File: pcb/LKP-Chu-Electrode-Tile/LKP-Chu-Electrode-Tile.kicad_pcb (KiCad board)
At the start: 2 copper layers, 19 parts, among them J1 Intercon, J10 Electrode 0, J11 Electrode 2, J12 Electrode 4, J13 Electrode 6, J14 Electrode 8, J15 Electrode 10, J16 Electrode 12, J17 Electrode 14, J2 Electrode 1, J3 Electrode 3, J4 Electrode 5, J5 Electrode 7, J6 Electrode 9, J7 Electrode 11, J8 Electrode 13, J9 Electrode 15

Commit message: Copper fills and fix solder mask on electrodes
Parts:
- J1: moved to B.Cu
- moved J1 201.1 mm to (240.6, 86.0)
- moved J6 144.1 mm to (217.2, 63.5)
- moved J8 133.4 mm to (113.2, 63.5)
- moved J5 117.4 mm to (243.2, 108.5)
- moved J10 106.7 mm to (61.2, 108.5)
- moved J16 98.3 mm to (139.2, 63.5)
- moved J4 93.5 mm to (191.2, 108.5)
- moved H1 89.2 mm to (33.5, 52.5)
- moved H2 89.2 mm to (20.6, 77.5)
- moved J9 87.0 mm to (61.2, 63.5)
- moved J11 83.4 mm to (113.2, 108.5)
- moved J14 75.3 mm to (243.2, 63.5)
- moved J7 75.3 mm to (165.2, 63.5)
- moved J3 71.2 mm to (139.2, 108.5)
- moved J12 62.2 mm to (165.2, 108.5)
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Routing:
- added copper zone on B.Cu, net (none)
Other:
- board outline added: 208.5 x 90 mm

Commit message: Place screw holes.
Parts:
- added H3: MountingHole, MountingHole:MountingHole_3.2mm_M3_ISO7380, F.Cu at (44.2, 86.0)
- moved H2 54.0 mm to (44.2, 126.0)
- moved H1 12.6 mm to (44.2, 46.0)
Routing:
- net Net-(J1-Pad10): track 0.00 -> 4.02 mm, vias 0 -> 1
- net Net-(J1-Pad9): track 0.00 -> 3.73 mm, vias 0 -> 1
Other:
- board size 208.5 x 90 mm -> 216 x 90 mm
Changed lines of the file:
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@@
   (general
     (thickness 1.6)
-    (drawings 7)
-    (tracks 0)
-    (modules 19)
+    (drawings 8)
+    (tracks 6)
+    (modules 20)
     (nets 18)
   )
@@
     (uvia_dia 0.3)
     (uvia_drill 0.1)
+  )
+  (module "MountingHole:MountingHole_3.2mm_M3_ISO7380" (layer "F.Cu")
+    (at 44.25 86)
+    (descr "Mounting Hole 3.2mm, no annular, M3, ISO7380")
+    (tags "mounting hole 3.2mm no annular m3 iso7380")
+    (attr virtual)
+    (fp_text reference "H3" (at 0 -3.85) (layer "F.SilkS") hide
+      (effects (font (size 1 1) (thickness 0.15)))
+    )
+    (fp_text value "MountingHole" (at 0 3.85) (layer "F.Fab")
+      (effects (font (size 1 1) (thickness 0.15)))
+    )
+    (fp_text user "%R" (at 0.3 0) (layer "F.Fab")
+      (effects (font (size 1 1) (thickness 0.15)))
+    )
+    (fp_circle (center 0 0) (end 2.85 0) (layer "Cmts.User") (width 0.15))
+    (fp_circle (center 0 0) (end 3.1 0) (layer "F.CrtYd") (width 0.05))
+    (pad "1" np_thru_hole circle (at 0 0) (size 3.2 3.2) (drill 3.2) (layers *.Cu *.Mask))
   )
   (module "private:CapSense_Electrode_25x44mm" (layer "F.Cu")
@@
   )
   (module "MountingHole:MountingHole_3.2mm_M3_ISO7380" (layer "F.Cu")
-    (at 20.65 77.45)
+    (at 44.25 126)
     (descr "Mounting Hole 3.2mm, no annular, M3, ISO7380")
     (tags "mounting hole 3.2mm no annular m3 iso7380")
@@
   )
   (module "MountingHole:MountingHole_3.2mm_M3_ISO7380" (layer "F.Cu")
-    (at 33.5 52.5)
+    (at 44.25 46)
     (descr "Mounting Hole 3.2mm, no annular, M3, ISO7380")
     (tags "mounting hole 3.2mm no annular m3 iso7380")
     (attr virtual)
-    (fp_text reference "H1" (at 0 -3.85) (layer "F.SilkS")
+    (fp_text reference "H1" (at 0 -3.85) (layer "F.SilkS") hide
       (effects (font (size 1 1) (thickness 0.15)))
     )
@@
     (pad "1" np_thru_hole circle (at 0 0) (size 3.2 3.2) (drill 3.2) (layers *.Cu *.Mask))
   )
-  (gr_line (start 47.75 131) (end 256.25 131) (layer "Edge.Cuts") (width 0.1))
-  (gr_line (start 47.75 41) (end 47.75 131) (layer "Edge.Cuts") (width 0.1))
-  (gr_line (start 256.25 41) (end 47.75 41) (layer "Edge.Cuts") (width 0.1))
+  (dimension 8 (width 0.1) (layer "Dwgs.User")
+    (gr_text "8.000 mm" (at 44.25 134.75) (layer "Dwgs.User")
+      (effects (font (size 1 1) (thickness 0.15)))
+    )
+    (feature1 (pts (xy 48.25 131) (xy 48.25 134.086421)))
+    (feature2 (pts (xy 40.25 131) (xy 40.25 134.086421)))
+    (crossbar (pts (xy 40.25 133.5) (xy 48.25 133.5)))
+    (arrow1a (pts (xy 48.25 133.5) (xy 47.123496 134.086421)))
+    (arrow1b (pts (xy 48.25 133.5) (xy 47.123496 132.913579)))
+    (arrow2a (pts (xy 40.25 133.5) (xy 41.376504 134.086421)))
+    (arrow2b (pts (xy 40.25 133.5) (xy 41.376504 132.913579)))
+  )
+  (gr_line (start 40.25 131) (end 256.25 131) (layer "Edge.Cuts") (width 0.1))
+  (gr_line (start 40.25 41) (end 40.25 131) (layer "Edge.Cuts") (width 0.1))
+  (gr_line (start 256.25 41) (end 40.25 41) (layer "Edge.Cuts") (width 0.1))
   (gr_line (start 256.25 131) (end 256.25 41) (layer "Edge.Cuts") (width 0.1))
   (dimension 15.625 (width 0.1) (layer "Dwgs.User")
@@
   )
   (dimension 90 (width 0.1) (layer "Dwgs.User")
-    (gr_text "90.000 mm" (at 45 86 90) (layer "Dwgs.User")
-      (effects (font (size 1 1) (thickness 0.15)))
-    )
-    (feature1 (pts (xy 61.25 41) (xy 45.663579 41)))
-    (feature2 (pts (xy 61.25 131) (xy 45.663579 131)))
-    (crossbar (pts (xy 46.25 131) (xy 46.25 41)))
-    (arrow1a (pts (xy 46.25 41) (xy 46.836421 42.126504)))
-    (arrow1b (pts (xy 46.25 41) (xy 45.663579 42.126504)))
-    (arrow2a (pts (xy 46.25 131) (xy 46.836421 129.873496)))
-    (arrow2b (pts (xy 46.25 131) (xy 45.663579 129.873496)))
-  )
+    (gr_text "90.000 mm" (at 38 86 90) (layer "Dwgs.User")
+      (effects (font (size 1 1) (thickness 0.15)))
+    )
+    (feature1 (pts (xy 40.25 41) (xy 38.663579 41)))
+    (feature2 (pts (xy 40.25 131) (xy 38.663579 131)))
+    (crossbar (pts (xy 39.25 131) (xy 39.25 41)))
+    (arrow1a (pts (xy 39.25 41) (xy 39.836421 42.126504)))
+    (arrow1b (pts (xy 39.25 41) (xy 38.663579 42.126504)))
+    (arrow2a (pts (xy 39.25 131) (xy 39.836421 129.873496)))
+    (arrow2b (pts (xy 39.25 131) (xy 38.663579 129.873496)))
+  )
+  (segment (start 238.1 86) (end 235.6 86) (width 0.25) (layer "B.Cu") (net 10))
+  (segment (start 235.6 86) (end 234.732 86.868) (width 0.25) (layer "B.Cu") (net 10))
+  (via (at 234.732 86.868) (size 0.8) (drill 0.4) (layers "F.Cu" "B.Cu") (net 10))
+  (segment (start 243.15 86) (end 245.887 86) (width 0.25) (layer "B.Cu") (net 9))
+  (segment (start 245.887 86) (end 246.797 85.09) (width 0.25) (layer "B.Cu") (net 9))
+  (via (at 246.797 85.09) (size 0.8) (drill 0.4) (layers "F.Cu" "B.Cu") (net 9))
   (zone (net 0) (net_name "") (layer "B.Cu") (hatch edge 0.508)
     (connect_pads (clearance 0.25))

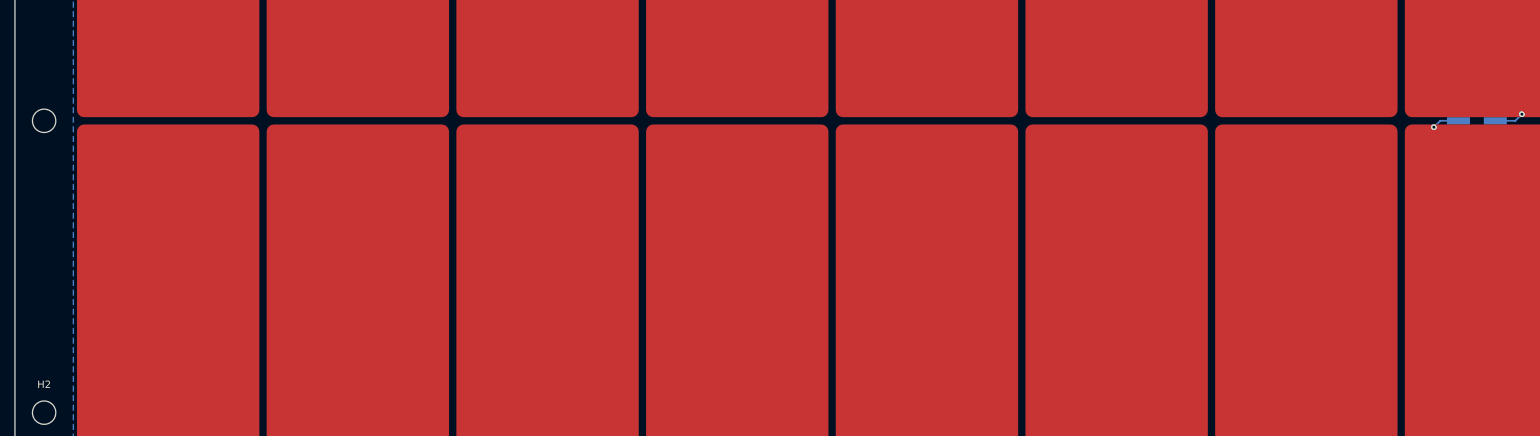
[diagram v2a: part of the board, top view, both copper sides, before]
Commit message: Finish routing.
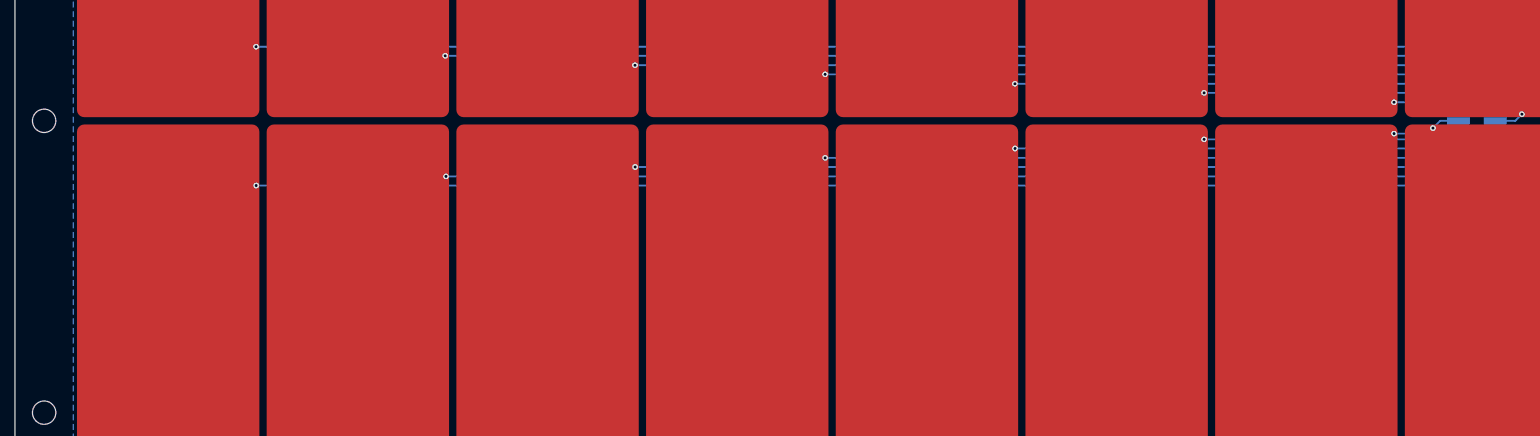
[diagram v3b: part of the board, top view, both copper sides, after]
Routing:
- net Net-(J1-Pad2): track 0.00 -> 170.4 mm, vias 0 -> 1
- net Net-(J1-Pad17): track 0.00 -> 164.8 mm, vias 0 -> 1
- net Net-(J1-Pad16): track 0.00 -> 144.5 mm, vias 0 -> 1
- net Net-(J1-Pad3): track 0.00 -> 138.8 mm, vias 0 -> 1
- net Net-(J1-Pad4): track 0.00 -> 118.4 mm, vias 0 -> 1
- net Net-(J1-Pad15): track 0.00 -> 112.9 mm, vias 0 -> 1
- net Net-(J1-Pad14): track 0.00 -> 92.4 mm, vias 0 -> 1
- net Net-(J1-Pad5): track 0.00 -> 86.8 mm, vias 0 -> 1
- net Net-(J1-Pad6): track 0.00 -> 66.4 mm, vias 0 -> 1
- net Net-(J1-Pad13): track 0.00 -> 60.8 mm, vias 0 -> 1
- net Net-(J1-Pad12): track 0.00 -> 40.4 mm, vias 0 -> 1
- net Net-(J1-Pad7): track 0.00 -> 34.9 mm, vias 0 -> 1
- net Net-(J1-Pad8): track 0.00 -> 14.6 mm, vias 0 -> 1
- net Net-(J1-Pad11): track 0.00 -> 8.83 mm, vias 0 -> 1
- added copper zone on B.Cu, net GNDA
- removed copper zone on B.Cu, net (none)
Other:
- board text added: "LKP-Chu Electrode Tile 2x8 V1.0"

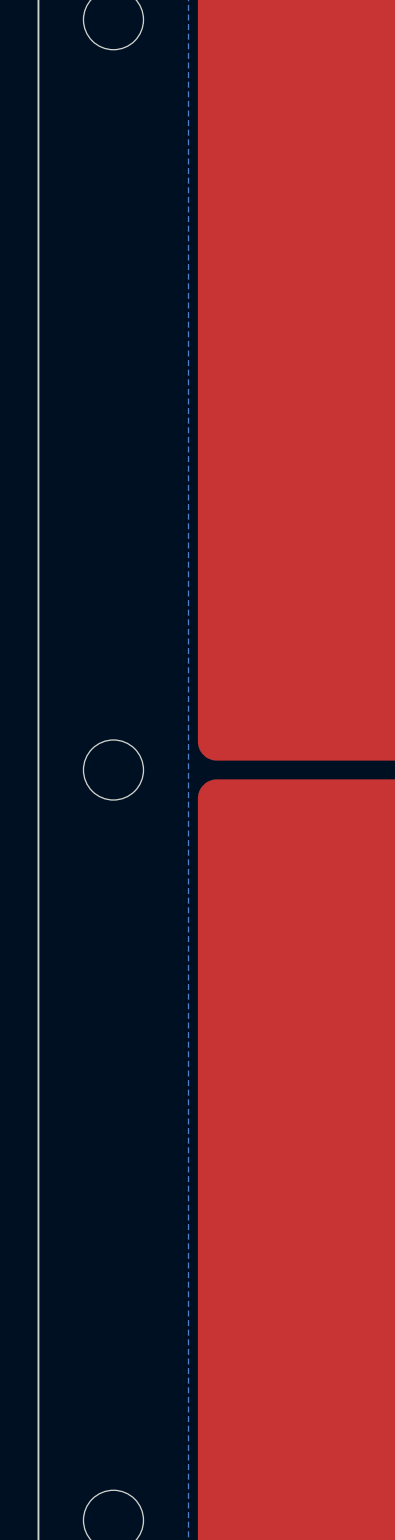
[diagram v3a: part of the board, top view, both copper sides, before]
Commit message: Add direction indicator.
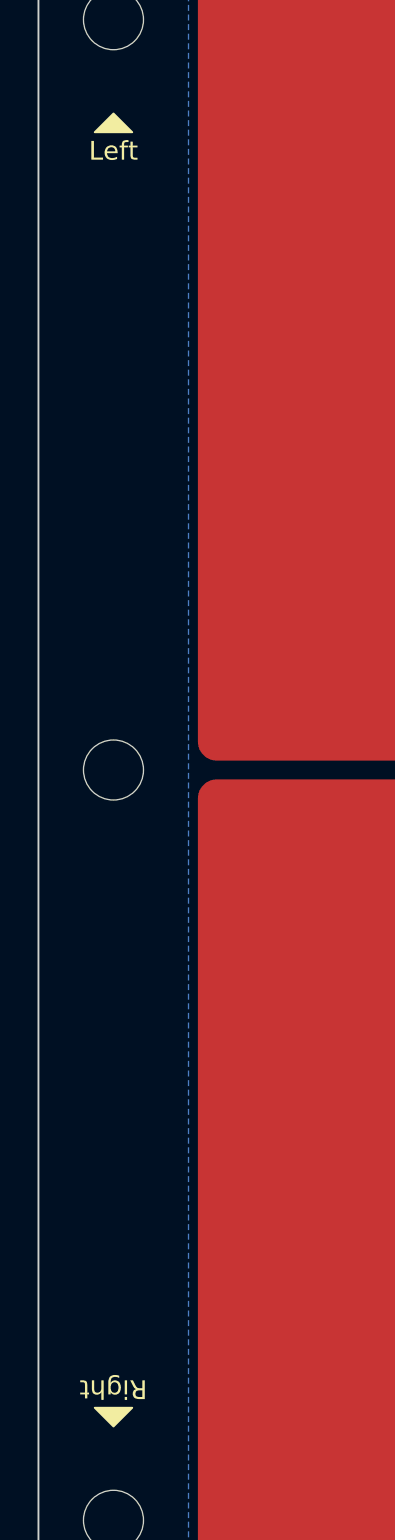
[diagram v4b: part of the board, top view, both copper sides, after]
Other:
- board text added: "Left"
- board text added: "Right"
